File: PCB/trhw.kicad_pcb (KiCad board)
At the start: 2 copper layers, 210 x 31 mm, 44 parts, among them J1 USB_C_Receptacle_USB2.0_14P, J2 Conn_01x02, J4 Conn_01x16, SW1 SW_Push, U1 RP2040, U2 W25Q32JVSS, U3 TPS63001, U4 Raspberry Pi Radio Module 2, U5 TP4056-42-ESOP8, Y1 Crystal_GND24

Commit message: Final
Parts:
- added C19: 100n, Capacitor_SMD:C_0402_1005Metric, F.Cu at (164.2, 50.7)
- added C20: 100n, Capacitor_SMD:C_0402_1005Metric, F.Cu at (172.3, 50.6)
- added C21: 100n, Capacitor_SMD:C_0402_1005Metric, F.Cu at (179.6, 50.7)
- added C22: 100n, Capacitor_SMD:C_0402_1005Metric, F.Cu at (187.0, 50.7)
- added D4: WS2812B, LED_SMD:LED_WS2812B_PLCC4_5.0x5.0mm_P3.2mm, F.Cu at (166.8, 54.0)
- added D5: WS2812B, LED_SMD:LED_WS2812B_PLCC4_5.0x5.0mm_P3.2mm, F.Cu at (174.2, 54.0)
- added D6: WS2812B, LED_SMD:LED_WS2812B_PLCC4_5.0x5.0mm_P3.2mm, F.Cu at (181.6, 54.0)
- added D7: WS2812B, LED_SMD:LED_WS2812B_PLCC4_5.0x5.0mm_P3.2mm, F.Cu at (189.0, 54.0)
- added GP5: SW_Push, Button_Switch_SMD:SW_SPST_B3U-1000P, F.Cu at (124.0, 41.0)
- added GP6: SW_Push, Button_Switch_SMD:SW_SPST_B3U-1000P, F.Cu at (130.0, 41.0)
- added GP7: SW_Push, Button_Switch_SMD:SW_SPST_B3U-1000P, F.Cu at (136.0, 41.0)
- added REF**: MountingHole_3.2mm_M3, MountingHole:MountingHole_3.2mm_M3, F.Cu at (113.5, 55.2)
- added REF**: MountingHole_2.2mm_M2, MountingHole:MountingHole_2.2mm_M2, F.Cu at (98.5, 55.2)
- added REF**: MountingHole_2.7mm_M2.5, MountingHole:MountingHole_2.7mm_M2.5, F.Cu at (106.0, 55.2)
- added Reset: SW_Push, Button_Switch_SMD:SW_SPST_B3U-1000P, F.Cu at (148.0, 41.0)
- moved R4 68.4 mm to (69.2, 58.1), turned to 90 degrees
- moved R7 68.0 mm to (52.9, 57.5), turned to 180 degrees
- moved SW1 68.0 mm to (72.8, 57.5)
- moved C1 67.3 mm to (85.6, 51.9)
- moved C10 67.3 mm to (78.4, 56.3)
- moved C11 67.3 mm to (72.1, 53.9)
- moved C12 67.3 mm to (70.1, 46.5)
- moved C13 67.3 mm to (71.1, 45.6)
- moved C14 67.3 mm to (62.5, 50.2)
- moved C15 67.3 mm to (52.5, 46.4)
- moved C16 67.3 mm to (57.1, 42.8)
- moved C17 67.3 mm to (53.3, 40.5)
- moved C18 67.3 mm to (53.7, 49.7)
- moved C2 67.3 mm to (88.1, 48.0)
- moved C3 67.3 mm to (83.6, 48.9)
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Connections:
- net Net-(D1-K) renamed VCC
- U1 pad 26: unconnected-(U1-RUN-Pad26) -> Net-(U1-RUN)
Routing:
- net GP4: track 0.00 -> 97.0 mm, vias 0 -> 2
- net Net-(U1-RUN): track 0.00 -> 76.3 mm, vias 0 -> 4
- net GP7: track 0.00 -> 66.0 mm, vias 0 -> 2
- net GP6: track 0.00 -> 60.5 mm, vias 0 -> 2
- net GP5: track 0.00 -> 53.2 mm, vias 0 -> 2
- net +3V3: track 294.8 -> 325.9 mm
- net GND: track 74.8 -> 58.2 mm, vias 17 -> 24
- net Net-(D5-DOUT): track 0.00 -> 13.7 mm
- net Net-(D4-DOUT): track 0.00 -> 13.7 mm
- net Net-(D6-DOUT): track 0.00 -> 13.7 mm
- net GP25: track 159.2 -> 171.8 mm
- net Net-(J1-CC1): track 0.00 -> 1.93 mm
- net GP23: track 170.6 -> 171.9 mm
- net Boot: track 17.7 -> 18.7 mm
- net Net-(D3-K): track 8.67 -> 7.67 mm
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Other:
- outline, holes or cut-outs redrawn
- board text added: "00"
- board text added: "0{dblquote}"
- board text added: "1 mile -- 1.609km 1km -- 1000m 1m -- 100cm 1cm -- 10mm"
- board text added: "1 mile -- 1760yd 1yd -- 3ft 1ft -- 12in 1in -- 25.4mm"
- board text added: "10"
- board text added: "100"
- board text added: "100 light-picoseconds"
- board text added: "10⁻¹²"
- board text added: "10⁻¹⁸ parsecs"
- board text added: "110"
- board text added: "120"
- board text added: "122.77mm"
- board text added: "122.81mm"
- board text added: "13.63mm"
- board text added: "130"
- board text added: "14.959787069mm"
- board text added: "140"
- board text added: "150"
- board text added: "160"
- board text added: "170"
- board text added: "180"
- board text added: "190"
- board text added: "1{dblquote}"
- board text added: "20"
- board text added: "200"
- board text added: "29.9792458mm"
- board text added: "2{dblquote}"
- board text added: "30"
- board text added: "30.69mm"
- board text added: "30.7mm"
- board text added: "30.856775813mm"
- board text added: "3{dblquote}"
- board text added: "40"
- board text added: "4{dblquote}"
- board text added: "5.5GHz"
- board text added: "50"
- board text added: "54.51mm"
- board text added: "5{dblquote}"
- board text added: "60"
- board text added: "6{dblquote}"
- board text added: "70"
- board text added: "7{dblquote}"
- board text added: "80"
- board text added: "8{dblquote}"
- board text added: "90"
- board text added: "Astronomical Units"
- board text added: "Bluetooth Middle Wavelength"
- board text added: "GP4"
- board text added: "M2"
- board text added: "M2.5"
- board text added: "M3"
- board text added: "Wifi Wavelength"
- board text added: "this ruler has wifi"
- board text added: "wifi thing"
- board text added: "λ/4"

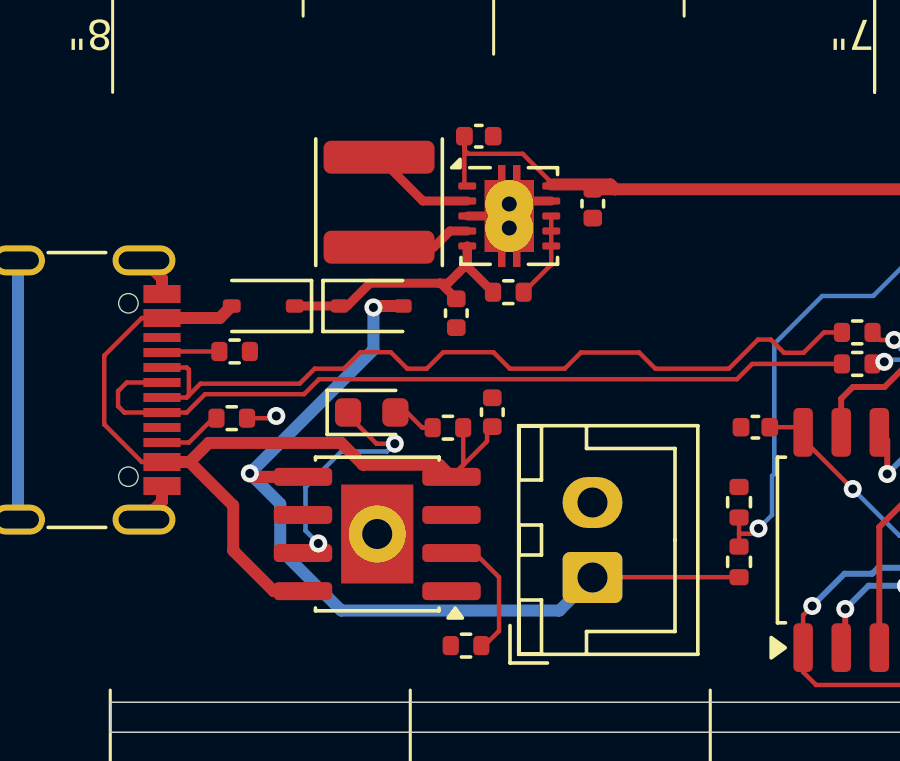
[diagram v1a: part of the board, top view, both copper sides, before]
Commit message: Thermal via fix
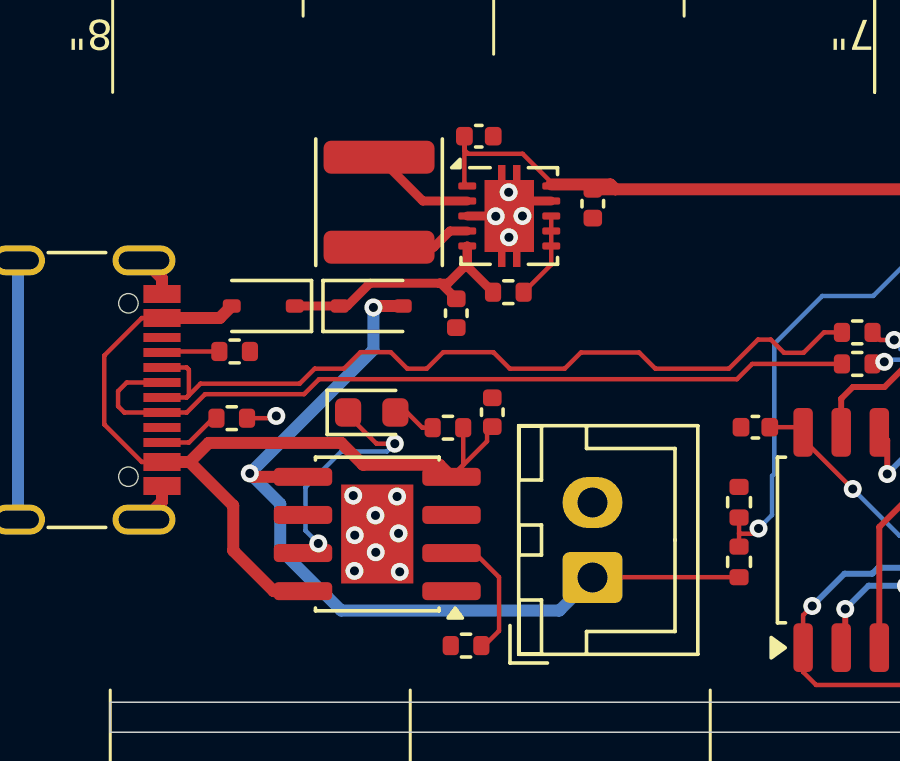
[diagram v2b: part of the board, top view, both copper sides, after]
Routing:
- net GND: track 58.2 -> 58.5 mm, vias 24 -> 36
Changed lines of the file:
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@@
 			(outputformat 1)
 			(mirror no)
-			(drillshape 1)
+			(drillshape 0)
 			(scaleselection 1)
 			(outputdirectory "")
@@
 			(zone_connect 2)
 		)
-		(pad "9" thru_hole circle
-			(at 0 0 270)
-			(size 1.905 1.905)
-			(drill 1)
-			(layers "*.Cu" "*.Mask")
-			(remove_unused_layers no)
-			(net 1 "GND")
-			(pinfunction "EPAD")
-			(pintype "passive")
-		)
 		(pad "9" smd rect
 			(at 0 0 180)
@@
 			(pintype "input")
 		)
-		(pad "11" thru_hole circle
-			(at 0 -0.4 90)
-			(size 1.6 1.6)
-			(drill 0.5)
-			(layers "*.Cu" "*.Mask")
-			(remove_unused_layers no)
-			(net 1 "GND")
-			(pinfunction "PGND")
-			(pintype "passive")
-		)
 		(pad "11" smd custom
 			(at 0 0)
@@
 			)
 		)
-		(pad "11" thru_hole circle
-			(at 0 0.4 90)
-			(size 1.6 1.6)
-			(drill 0.5)
-			(layers "*.Cu" "*.Mask")
-			(remove_unused_layers no)
-			(net 1 "GND")
-			(pinfunction "PGND")
-			(pintype "passive")
-		)
 		(embedded_fonts no)
 		(model "C:/Users/nimit/Desktop/Projects/kicadfp/3dmodels/TPS63001DRCR.STEP"
@@
 	)
 	(segment
-		(start 54.8 42.7)
-		(end 54.3 43.2)
-		(width 0.3)
-		(layer "F.Cu")
-		(net 1)
-	)
-	(segment
 		(start 228.038 49)
 		(end 226.754 47.716)
@@
 	)
 	(segment
+		(start 52.9 43.2)
+		(end 54.039997 43.2)
+		(width 0.3)
+		(layer "F.Cu")
+		(net 1)
+	)
+	(segment
 		(start 85.56 52.37)
 		(end 86.63 52.37)
@@
 	)
 	(segment
+		(start 54.8 42.7)
+		(end 55.7 42.7)
+		(width 0.3)
+		(layer "F.Cu")
+		(net 1)
+	)
+	(segment
 		(start 42.725 52.72)
 		(end 42.125 53.32)
@@
 	)
 	(segment
-		(start 52.9 43.2)
-		(end 53.725 43.2)
+		(start 54.3 43.2)
+		(end 54.8 42.7)
 		(width 0.3)
 		(layer "F.Cu")
@@
 	)
 	(segment
-		(start 55.7 42.7)
-		(end 54.8 42.7)
-		(width 0.3)
-		(layer "F.Cu")
-		(net 1)
-	)
-	(segment
 		(start 77.4 50.5625)
 		(end 77.4 51.3)
@@
 	)
 	(via
+		(at 49.15 53.84)
+		(size 0.6)
+		(drill 0.3)
+		(layers "F.Cu" "B.Cu")
+		(net 1)
+	)
+	(via
 		(at 81.7 57)
 		(size 0.6)
@@
 	)
 	(via
+		(at 50.65 55.06)
+		(size 0.6)
+		(drill 0.3)
+		(layers "F.Cu" "B.Cu")
+		(net 1)
+	)
+	(via
 		(at 75.62 52.75)
 		(size 0.6)
@@
 	)
 	(via
+		(at 49.84 53.18)
+		(size 0.6)
+		(drill 0.3)
+		(layers "F.Cu" "B.Cu")
+		(net 1)
+	)
+	(via
+		(at 50.56 52.55)
+		(size 0.6)
+		(drill 0.3)
+		(layers "F.Cu" "B.Cu")
+		(net 1)
+	)
+	(via
+		(at 54.29 43.91)
+		(size 0.6)
+		(drill 0.3)
+		(layers "F.Cu" "B.Cu")
+		(net 1)
+	)
+	(via
 		(at 87.054 43.144)
 		(size 0.6)
@@
 	)
 	(via
+		(at 54.74 43.2)
+		(size 0.6)
+		(drill 0.3)
+		(layers "F.Cu" "B.Cu")
+		(net 1)
+	)
+	(via
+		(at 49.14 55.03)
+		(size 0.6)
+		(drill 0.3)
+		(layers "F.Cu" "B.Cu")
+		(net 1)
+	)
+	(via
+		(at 50.61 53.78)
+		(size 0.6)
+		(drill 0.3)
+		(layers "F.Cu" "B.Cu")
+		(net 1)
+	)
+	(via
 		(at 90.21 48.95)
 		(size 0.6)
@@
 	)
 	(via
+		(at 53.85 43.21)
+		(size 0.6)
+		(drill 0.3)
+		(layers "F.Cu" "B.Cu")
+		(net 1)
+	)
+	(via
 		(at 229.825 44.7)
 		(size 0.6)
@@
 	)
 	(via
+		(at 54.28 42.41)
+		(size 0.6)
+		(drill 0.3)
+		(layers "F.Cu" "B.Cu")
+		(net 1)
+	)
+	(via
 		(at 74.354 42.128)
 		(size 0.6)
@@
 	)
 	(via
+		(at 49.85 54.41)
+		(size 0.6)
+		(drill 0.3)
+		(layers "F.Cu" "B.Cu")
+		(net 1)
+	)
+	(via
 		(at 106.8 47.6)
 		(size 0.6)
@@
 		(net 1)
 	)
+	(via
+		(at 49.1 52.52)
+		(size 0.6)
+		(drill 0.3)
+		(layers "F.Cu" "B.Cu")
+		(net 1)
+	)
